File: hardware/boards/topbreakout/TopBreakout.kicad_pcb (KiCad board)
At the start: 2 copper layers, 75.6 x 73 mm, 52 parts, among them J1 WURTH_ELECTRONICS_61400413321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, J2 MOLEX_52892-3033MOLEX_52892-3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, J3 USB-A-S-X-X-VT, J4 ST7735_1.4, U1 ANALOG_DEVICES_AD7606BSTZANAL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, U3 ANALOG_DEVICES_AD5754BREZANAL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, U5 MICROCHIP_MCP1700T-2502E-TTMI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

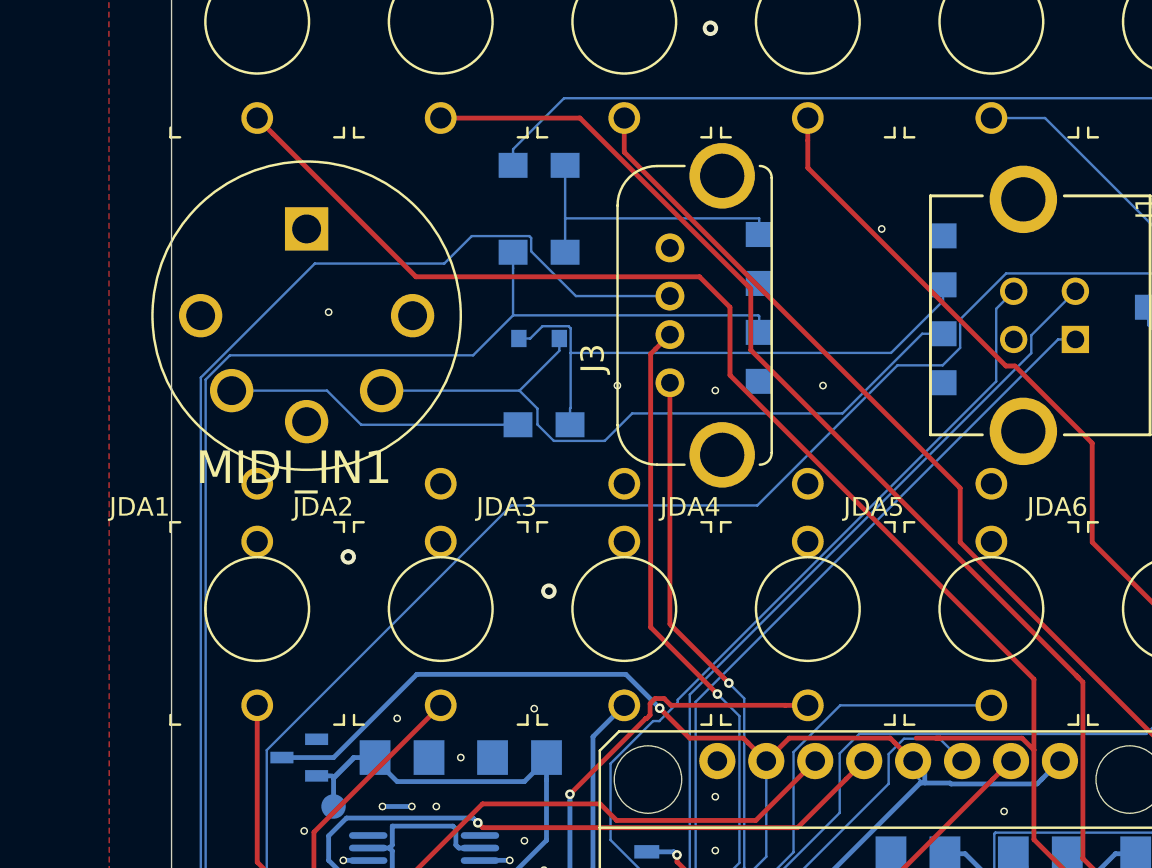
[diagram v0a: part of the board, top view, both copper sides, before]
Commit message: topbreakout changes
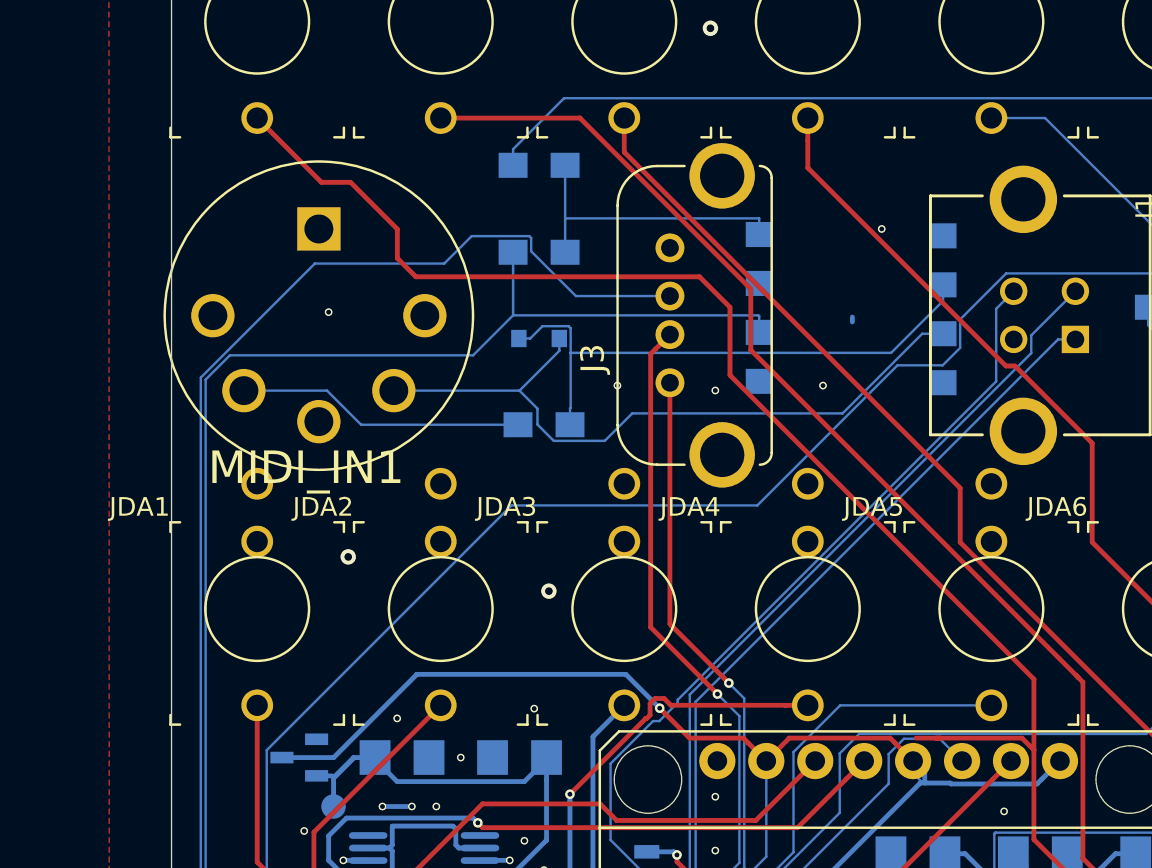
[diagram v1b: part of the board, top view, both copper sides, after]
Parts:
- moved MIDI_IN1 0.64 mm to (118.4, 91.4)
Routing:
- net AD_V1: track 86.2 -> 87.1 mm

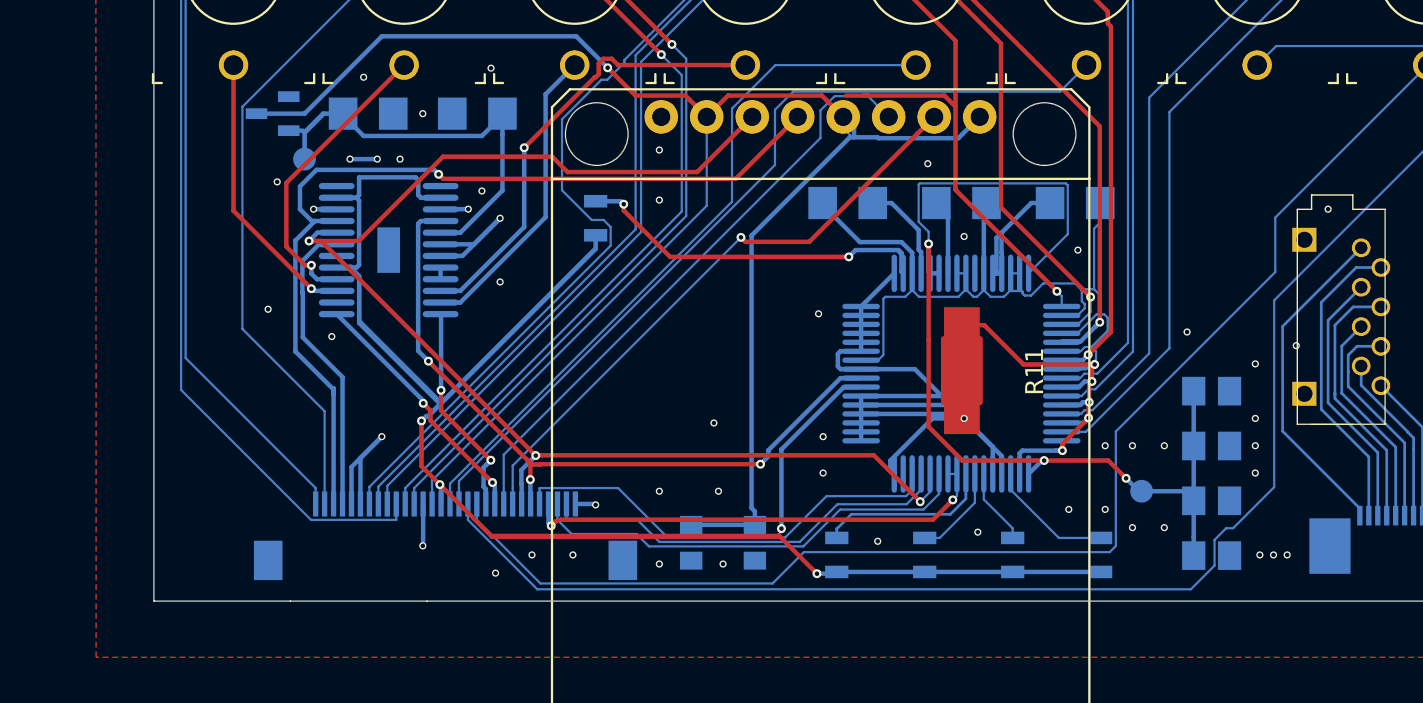
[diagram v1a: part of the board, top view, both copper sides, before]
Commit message: mainboard: add panel silkscreen to footprint of 6.5mm jack
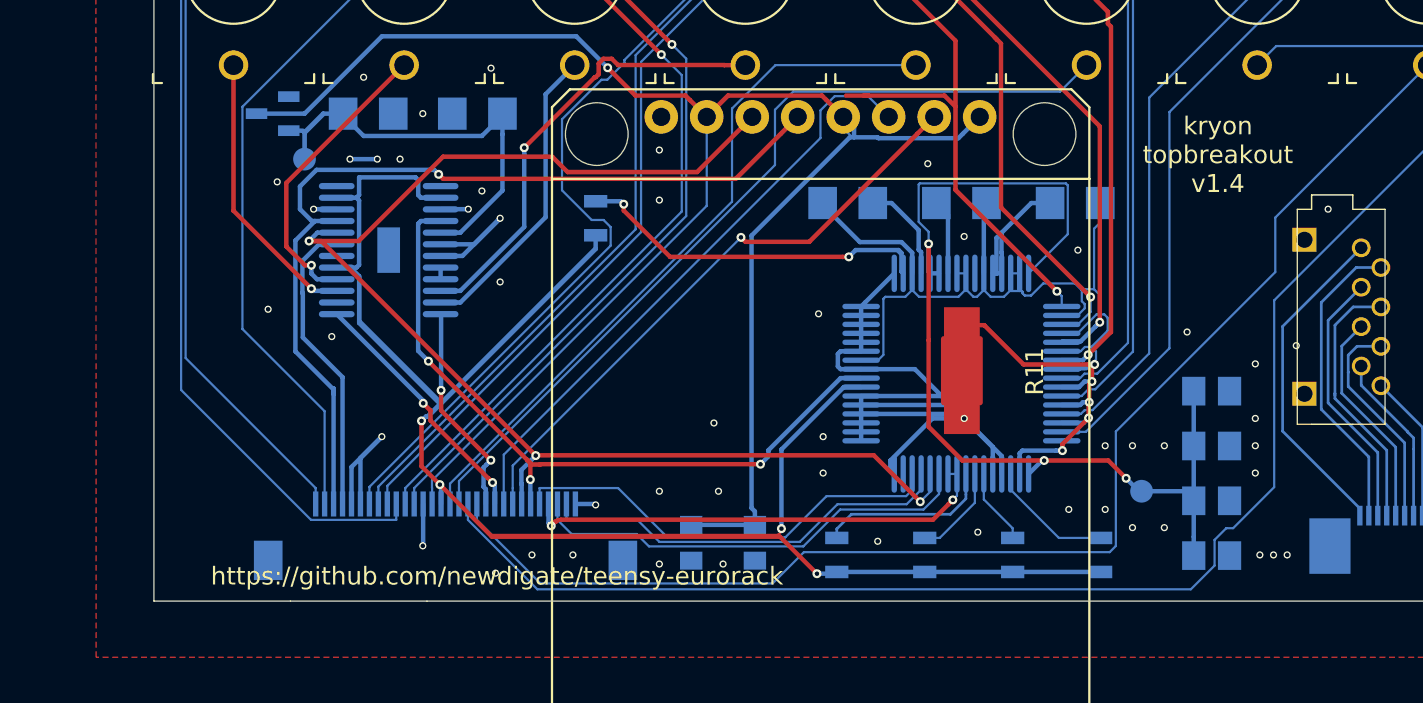
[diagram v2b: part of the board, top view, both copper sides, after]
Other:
- board text added: "https://github.com/newdigate/teensy-eurorack"
- board text added: "kryon topbreakout v1.4"

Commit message: revision 1.4 changes
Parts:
- C5, C7, C8: footprint topbreakout:1206 -> Capacitor_SMD:C_0805_2012Metric
- C6, C9: footprint topbreakout:C1206 -> Capacitor_SMD:C_0805_2012Metric
- R11: footprint Oddities:NetTie-I_Connected_SMD -> Mainboard:NetTie-I_Connected_SMD_small
- U$2: footprint topbreakout:TE_1-1734592-8 -> common:HFW8R-1STE1LF
- moved R2 24.7 mm to (148.8, 81.0)
- moved U5 23.2 mm to (139.7, 120.4), turned to 0 degrees
- moved D1 21.2 mm to (149.1, 83.8), turned to 180 degrees
- moved TP3 17.8 mm to (135.4, 124.2)
- moved C9 12.1 mm to (133.9, 118.9), turned to 180 degrees
- moved R7 10.6 mm to (143.3, 127.3)
- moved C6 9.16 mm to (133.9, 121.9)
- moved U$2 4.19 mm to (176.5, 136.1)
- turned R3 to 180 degrees
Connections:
- J2 pad 16: 3V3 -> +3V3
- J2 pad 17: VIN -> +3V3
- J2 pad 18: GND -> VIN
- J2 pad 19: /FPC connector/USB_A_VCC -> VIN
- J2 pad 20: /FPC connector/USB_A_D- -> GND
- J2 pad 21: /FPC connector/USB_A_D+ -> DA_SYNC
- J2 pad 22: /FPC connector/USB_B_VCC -> SPI0_MOSI
- J2 pad 23: /FPC connector/USB_B_D- -> MIDI_TX
- J2 pad 24: /FPC connector/USB_B_D+ -> MIDI_RX
- J2 pad 25: GND -> /FPC connector/USB_A_VCC
- J2 pad 26: GND -> /FPC connector/USB_A_D-
- J2 pad 27: DA_SYNC -> /FPC connector/USB_A_D+
- J2 pad 28: SPI0_MOSI -> /FPC connector/USB_B_VCC
- J2 pad 29: MIDI_TX -> /FPC connector/USB_B_D-
- J2 pad 30: MIDI_RX -> /FPC connector/USB_B_D+
- R10 pad 1: 3V3 -> +3V3
- R4 pad 1: 3V3 -> +3V3
- R7 pad 2: 3V3 -> +3V3
- R8 pad 1: 3V3 -> +3V3
- R9 pad 2: 3V3 -> +3V3
- U1 pad 23: 3V3 -> +3V3
- U3 pad 11: 3V3 -> +3V3
- U3 pad 14: 3V3 -> +3V3
- U3 pad 5: 3V3 -> +3V3
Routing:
- net +3V3: track 15.4 -> 187.0 mm, vias 0 -> 4
- net 3V3: track 140.5 -> 0.00 mm, vias 4 -> 0
- net /AD7606/AD_AGND: track 89.6 -> 191.6 mm, vias 5 -> 4
- net VIN: track 103.4 -> 68.5 mm, vias 1 -> 2
- net AD_V5: track 57.0 -> 88.8 mm, vias 0 -> 2
- net GATE_3: track 89.9 -> 58.3 mm, vias 0 -> 1
- net /FPC connector/USB_A_D+: track 80.1 -> 52.1 mm
- net MIDI_IN_PIN5: track 15.6 -> 40.0 mm, vias 0 -> 1
- net /AD7606/AVIN: track 63.0 -> 41.1 mm
- net MIDI_TX: track 84.9 -> 63.2 mm
- net Net-(D1-Pad1): track 29.3 -> 9.24 mm
- net AD_V3: track 59.6 -> 75.9 mm
- net AD_V4: track 57.5 -> 73.5 mm, vias 1 -> 0
- net /FPC connector/USB_A_VCC: track 61.8 -> 47.2 mm, vias 1 -> 0
- net SPI0_MISO: track 54.3 -> 41.9 mm, vias 3 -> 2
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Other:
- net class Default: via_dia 0.8 -> 0.4; via_drill 0.4 -> 0.25
- net class PWR added: clearance 0.18, trace_width 0.3, via_dia 0.5, via_drill 0.3
